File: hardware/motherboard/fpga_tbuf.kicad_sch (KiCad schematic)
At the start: 6 parts, among them U8 SN74ALVC164245

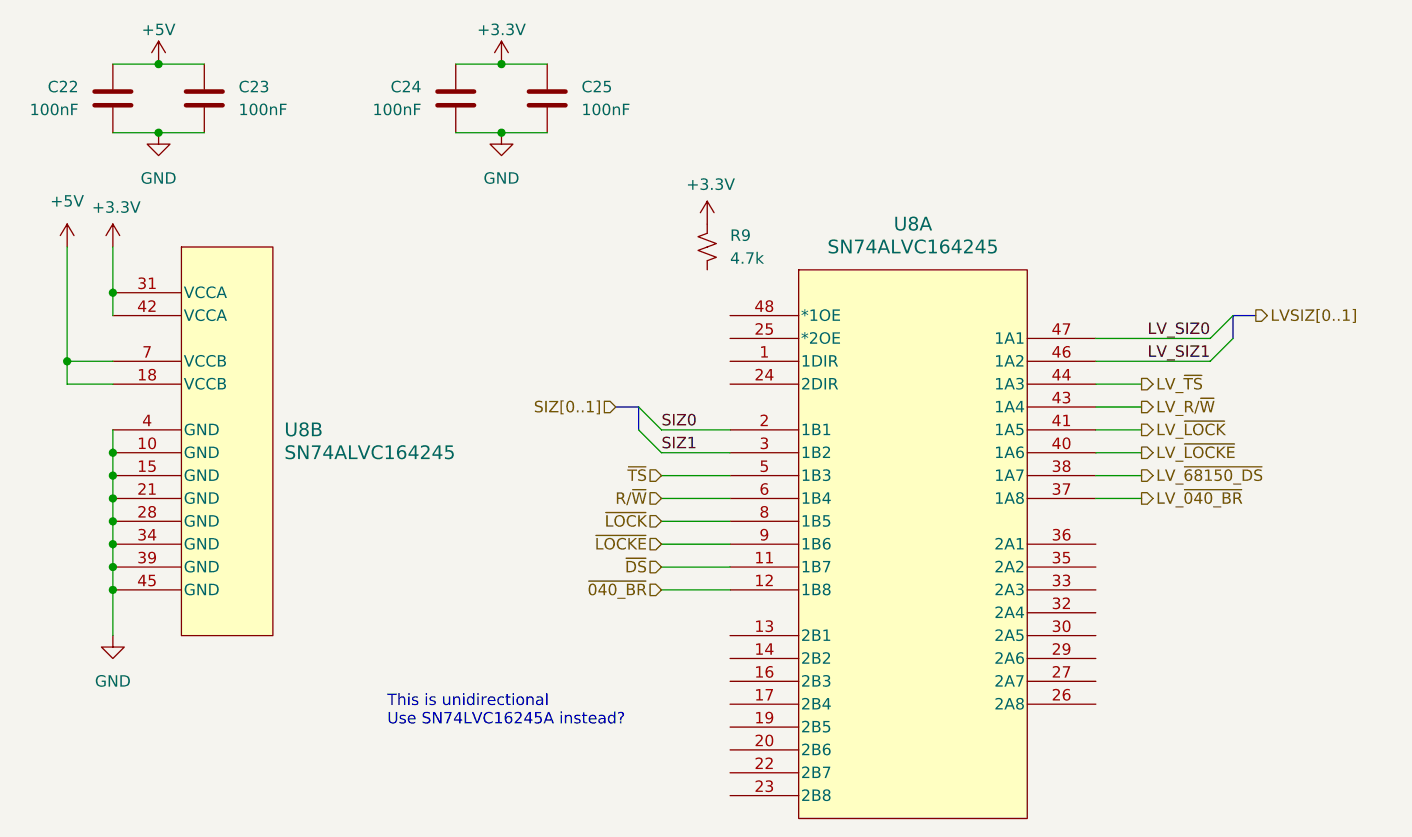
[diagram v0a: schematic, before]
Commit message: restructure, create minimum board project
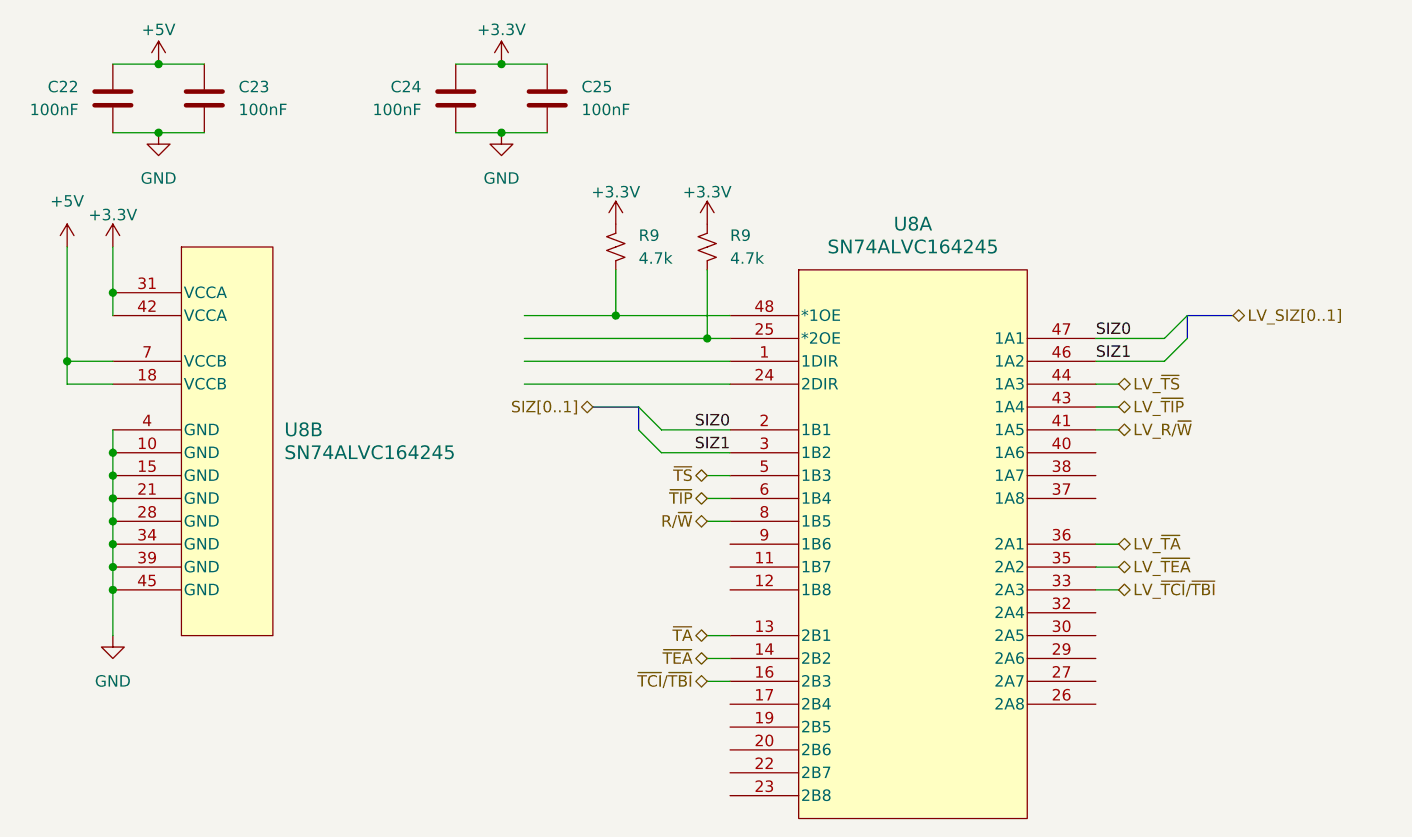
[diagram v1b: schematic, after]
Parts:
- added R9: 4.7k, symbol Device:R_Small_US
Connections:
- net +3V3 is gone; now on net +3.3V: R9.1, U8.31 (VCCA), U8.42 (VCCA)
- net LV_SIZ0 is gone; now on net SIZ0: U8.47 (1A1)
- net LV_SIZ1 is gone; now on net SIZ1: U8.46 (1A2)
- net LV_~{LOCK} is gone; now on net LV_R/~{W}: U8.41 (1A5)
- net ~{LOCK} is gone; now on net R/~{W}: U8.8 (1B5)
- net +3.3V: now also R9.1
- net LV_R/~{W}: no longer U8.43 (1A4)
- net R/~{W}: no longer U8.6 (1B4)
- net at R9.2: now also U8.25 (*2OE)
- net ~{TA}: now reaches U8.13 (2B1)
- net ~{TEA}: now reaches U8.14 (2B2)
- net ~{TCI}/~{TBI}: now reaches U8.16 (2B3)
- net LV_~{TCI}/~{TBI}: now reaches U8.33 (2A3)
- net LV_~{TEA}: now reaches U8.35 (2A2)
- net LV_~{TA}: now reaches U8.36 (2A1)
- net at U8.48 (*1OE): now also R9.2
- net LV_~{040_BR}: no longer names the net of U8.37 (1A8)
- net LV_~{68150_DS}: no longer names the net of U8.38 (1A7)
- net LV_~{LOCKE}: no longer names the net of U8.40 (1A6)
- net ~{040_BR}: no longer names the net of U8.12 (1B8)
- net ~{DS}: no longer names the net of U8.11 (1B7)
- net ~{LOCKE}: no longer names the net of U8.9 (1B6)
- new net LV_~{TIP}: U8.43 (1A4)
- new net ~{TIP}: U8.6 (1B4)
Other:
- note removed: "This is unidirectional Use SN74LVC16245A instead?"

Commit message: work on testboard, move 3d models
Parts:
- renumbered C22 to C28, C23 to C29, C24 to C30, C25 to C31, R9 to R26
